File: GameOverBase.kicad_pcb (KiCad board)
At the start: 4 copper layers, 50 x 35 mm, 47 parts, among them J1 USB_C_DEALON-USB-US31-106, J2 Serial Port, J3 add-on conn, Q1 PMN48XP, SW1 SW_DIP_x08, SW2 boot, SW3 Reset, U1 ESP32-WROOM-E, U2 4021, U3 MCP73831-2ACI-OT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

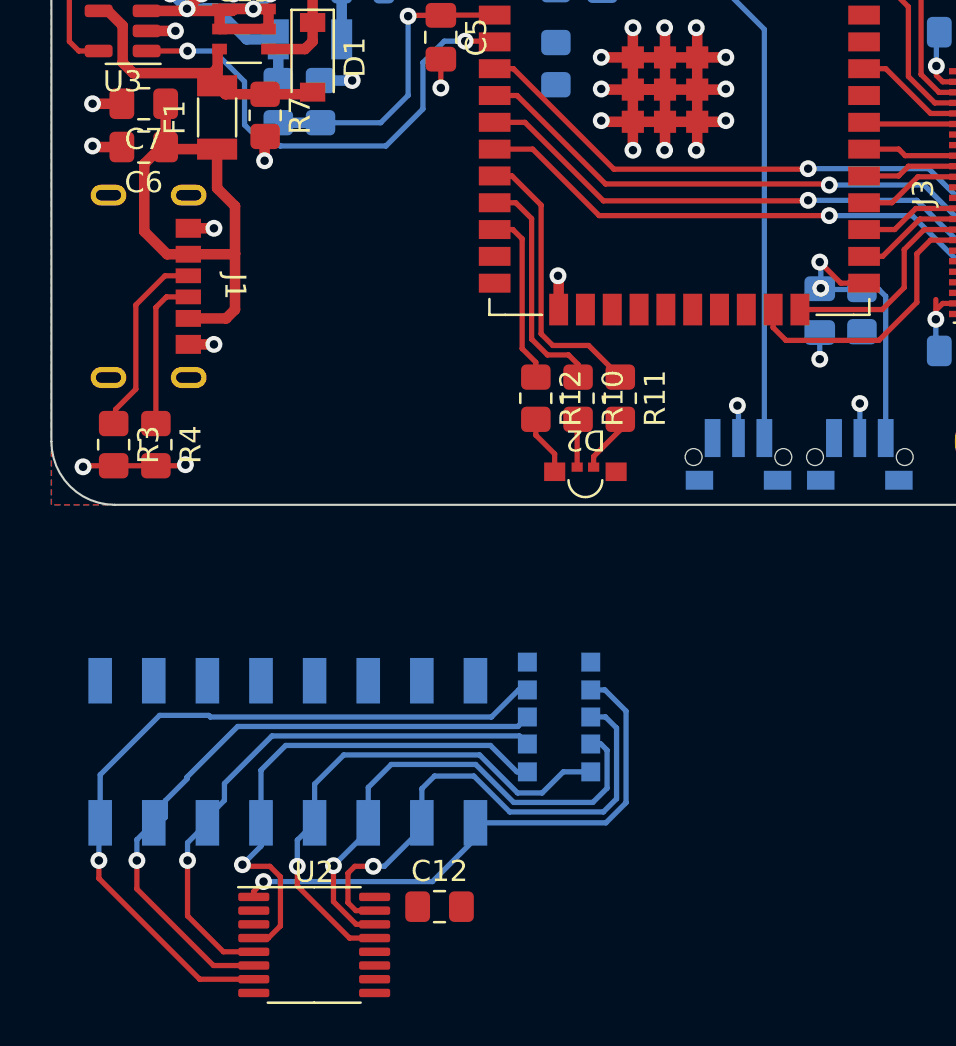
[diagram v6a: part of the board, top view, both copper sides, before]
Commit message: Routes DIP switches for device ID
This is not a nice route at all, and required changing the pins for the
resistor network in the schematics to make routing a bit easier.
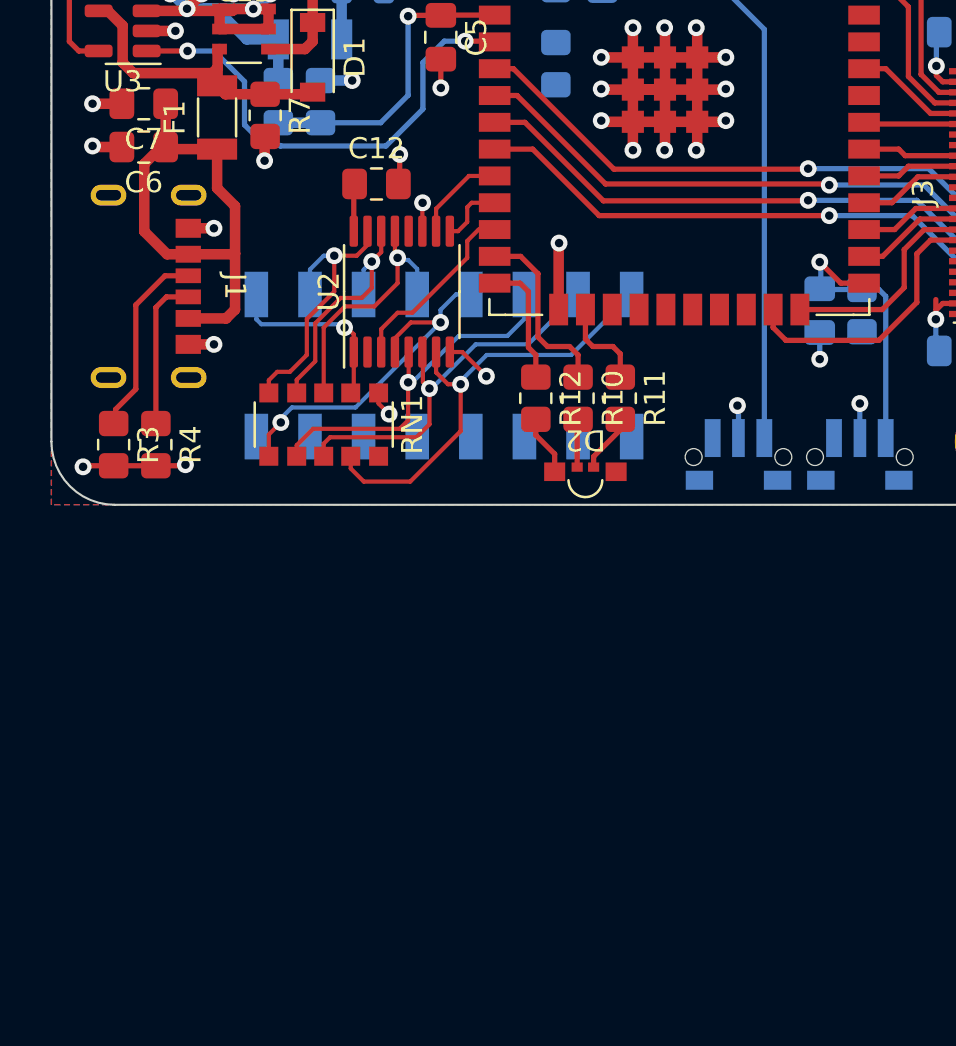
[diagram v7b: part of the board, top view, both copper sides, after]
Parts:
- J1: value USB_C_DEALON-USB-US31-106 -> locked
- RN1: moved to F.Cu
- moved C12 34.4 mm to (135.4, 99.8)
- moved U2 31.2 mm to (136.6, 104.9), turned to 90 degrees
- moved SW1 19.7 mm to (138.6, 108.4), turned to 90 degrees
- moved RN1 17.8 mm to (132.9, 111.2), turned to -90 degrees
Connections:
- RN1 pad 5: Net-(RN1-R4) -> Net-(U2-D6)
- SW1 pad 10: Net-(RN1-R2) -> Net-(U2-D6)
- SW1 pad 12: Net-(RN1-R4) -> Net-(RN1-R2)
- U1 pad 10: BAT_IND_G -> ID_CLK
- U1 pad 11: BAT_IND_R -> ID_LATCH
- U1 pad 12: BAT_IND_B -> ID_DATA
- U1 pad 13: ID_CLK -> BAT_IND_R
- U1 pad 14: ID_LATCH -> BAT_IND_B
- U1 pad 16: ID_DATA -> BAT_IND_G
- U2 pad 13: Net-(RN1-R4) -> Net-(RN1-R2)
- U2 pad 15: Net-(RN1-R2) -> Net-(U2-D6)
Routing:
- net Net-(RN1-R4): track 24.7 -> 0.00 mm, vias 1 -> 0
- net Net-(RN1-R1): track 26.5 -> 8.92 mm
- net Net-(RN1-R8): track 36.2 -> 21.6 mm
- net Net-(U2-D6): track 0.00 -> 13.2 mm, vias 0 -> 1
- net Net-(RN1-R7): track 30.8 -> 18.4 mm
- net Net-(RN1-R3): track 24.0 -> 11.6 mm
- net Net-(RN1-R2): track 24.3 -> 12.8 mm
- net BAT_IND_G: track 13.5 -> 4.44 mm
- net ID_DATA: track 0.00 -> 8.88 mm
- net Net-(RN1-R6): track 26.3 -> 17.4 mm
- net GND: track 98.1 -> 105.8 mm, vias 42 -> 46
- net Net-(RN1-R5): track 24.3 -> 16.9 mm, vias 1 -> 2
- net ID_CLK: track 0.00 -> 4.48 mm
- net ID_LATCH: track 0.00 -> 3.09 mm
- net BAT_IND_R: track 11.1 -> 8.69 mm
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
